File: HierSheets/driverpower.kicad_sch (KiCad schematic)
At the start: 0 parts

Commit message: .
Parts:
- added D1: 1.5SMCxxCA, Diode_SMD:D_SMC, symbol Diode:1.5SMCxxCA
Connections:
- new net GNDPWR: D1.1 (A1)
- new net IN: D1.2 (A2)

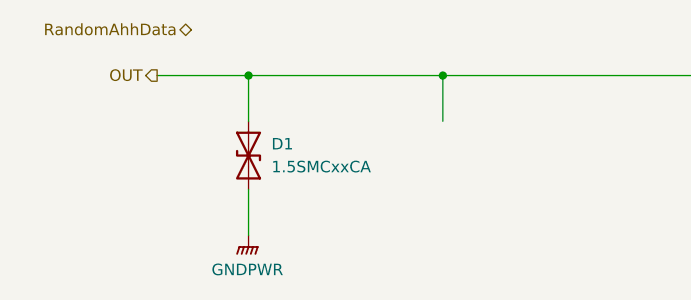
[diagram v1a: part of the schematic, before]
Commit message: Added kicker, interrupt, I2C pullups, buck converter, button
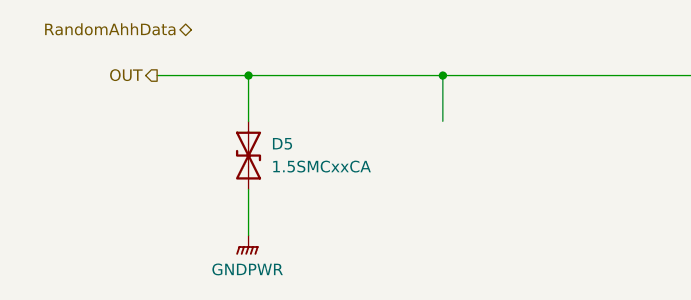
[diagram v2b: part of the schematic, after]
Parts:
- renumbered D1 to D5
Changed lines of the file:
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@@
 		(dnp no)
 		(fields_autoplaced yes)
-		(property "Reference" "D1"
+		(property "Reference" "D5"
 			(at 104.14 140.9699 90)
 			(show_name no)
@@
 			(project "Prototyp_0.1"
 				(path "/607d4431-9cfb-431e-bb0d-e8da578e6786/38f20ae7-a2c1-4edb-b66b-4d7ed02f4c65"
-					(reference "D1")
+					(reference "D5")
 					(unit 1)
 				)
@@
 		(dnp no)
 		(fields_autoplaced yes)
-		(property "Reference" "#PWR034"
+		(property "Reference" "#PWR039"
 			(at 101.6 156.21 0)
 			(hide yes)
@@
 			(project "Prototyp_0.1"
 				(path "/607d4431-9cfb-431e-bb0d-e8da578e6786/38f20ae7-a2c1-4edb-b66b-4d7ed02f4c65"
-					(reference "#PWR034")
+					(reference "#PWR039")
 					(unit 1)
 				)
